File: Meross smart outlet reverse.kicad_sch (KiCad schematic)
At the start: 0 parts

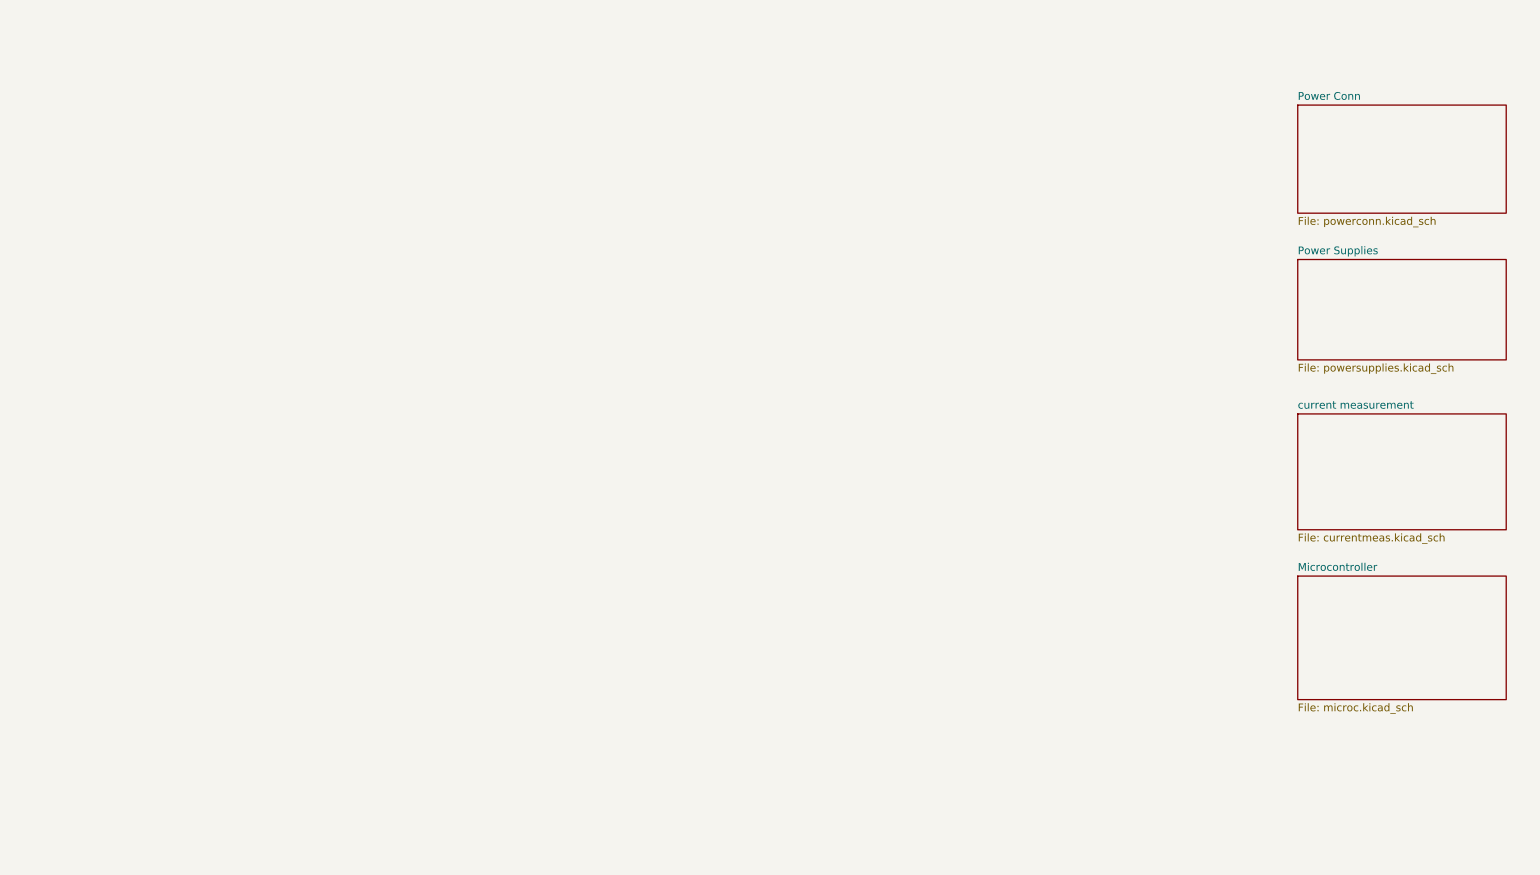
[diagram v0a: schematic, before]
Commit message: Making board layout match better. Added new footprints and symbols.
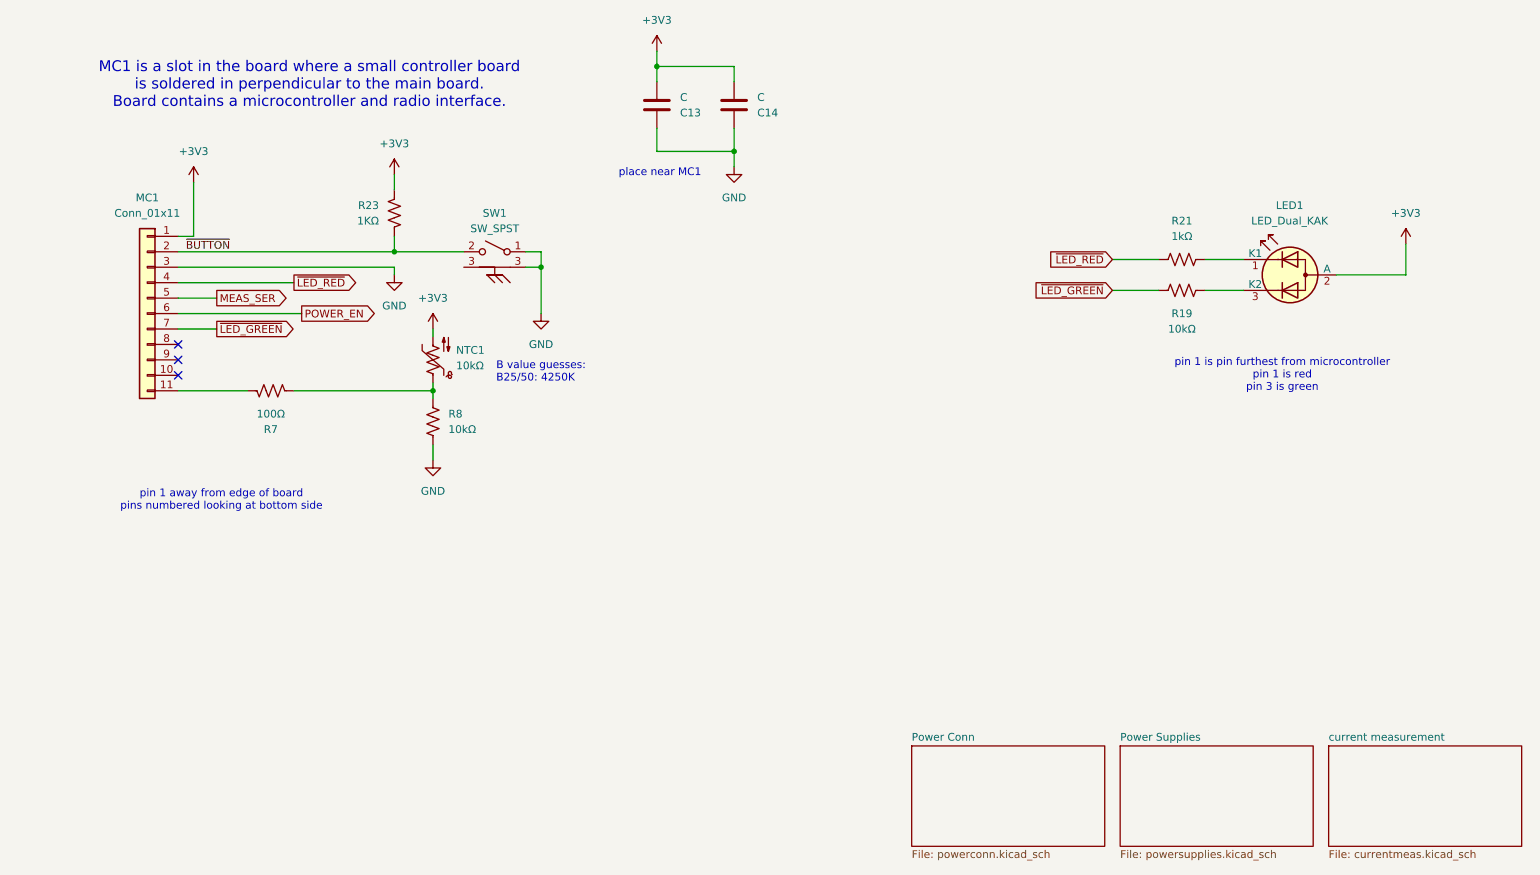
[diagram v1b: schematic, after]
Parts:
- added C13, C14: C, Capacitor_SMD:C_0402_1005Metric, symbol Device:C
- added LED1: LED_Dual_KAK, LED_THT:LED_D3.0mm-3, symbol Device:LED_Dual_KAK
- added MC1: Conn_01x11, HF relays:BoardToBoardInterface_11xP1.00mm, symbol Connector_Generic:Conn_01x11
- added NTC1: 10kΩ, Resistor_SMD:R_0402_1005Metric, symbol Device:Thermistor_NTC_US
- added R19, R8: 10kΩ, Resistor_SMD:R_0402_1005Metric, symbol Device:R_US
- added R21: 1kΩ, Resistor_SMD:R_0402_1005Metric, symbol Device:R_US
- added R23: 1KΩ, Resistor_SMD:R_0402_1005Metric, symbol Device:R_US
- added R7: 100Ω, Resistor_SMD:R_0402_1005Metric, symbol Device:R_US
- added SW1: SW_SPST, HF relays:SW_SPST_Omron_B3F-315x_Angled, symbol merossspecific:SW_SPST_Frame
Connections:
- new net: NTC1.1, R7.2, R8.2
- new net: LED1.1 (K1), R21.2
- new net: LED1.3 (K2), R19.2
- new net: MC1.11 (Pin_11), R7.1
- new net +3V3: C13.2, C14.2, LED1.2 (A), MC1.1 (Pin_1), NTC1.2, R23.1
- new net GND: C13.1, C14.1, MC1.3 (Pin_3), R8.1, SW1.1 (A), SW1.3
- new net MEAS_SER: MC1.5 (Pin_5)
- new net POWER_EN: MC1.6 (Pin_6)
- new net ~{BUTTON}: MC1.2 (Pin_2), R23.2, SW1.2 (B)
- new net ~{LED_GREEN}: MC1.7 (Pin_7), R19.1
- new net ~{LED_RED}: MC1.4 (Pin_4), R21.1
- no-connect marks 0 -> 3
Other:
- removed sheet Microcontroller
- note added: "B value guesses: B25/50: 4250K"
- note added: "MC1 is a slot in the board where a small controller board is soldered in perpendicular to the main board. Board contains a microcontroller and radio interface."
- note added: "pin 1 away from edge of board pins numbered looking at bottom side"
- note added: "pin 1 is pin furthest from microcontroller pin 1 is red pin 3 is green"
- note added: "place near MC1"
- title: (none) -> sensing and controlling interface

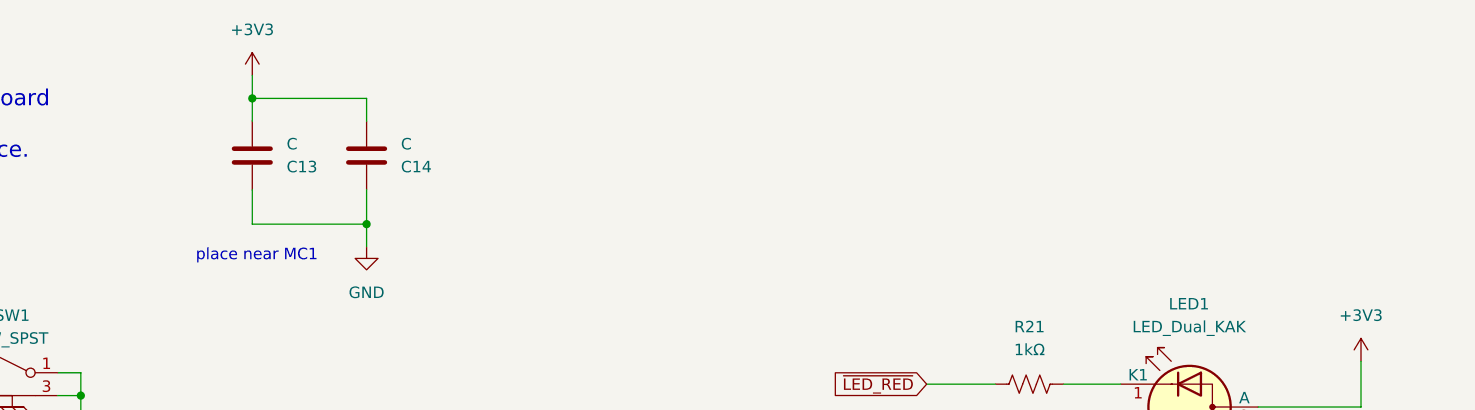
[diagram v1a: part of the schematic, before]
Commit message: All values determined for schematic. From measurements, datasheets, or reading markings.
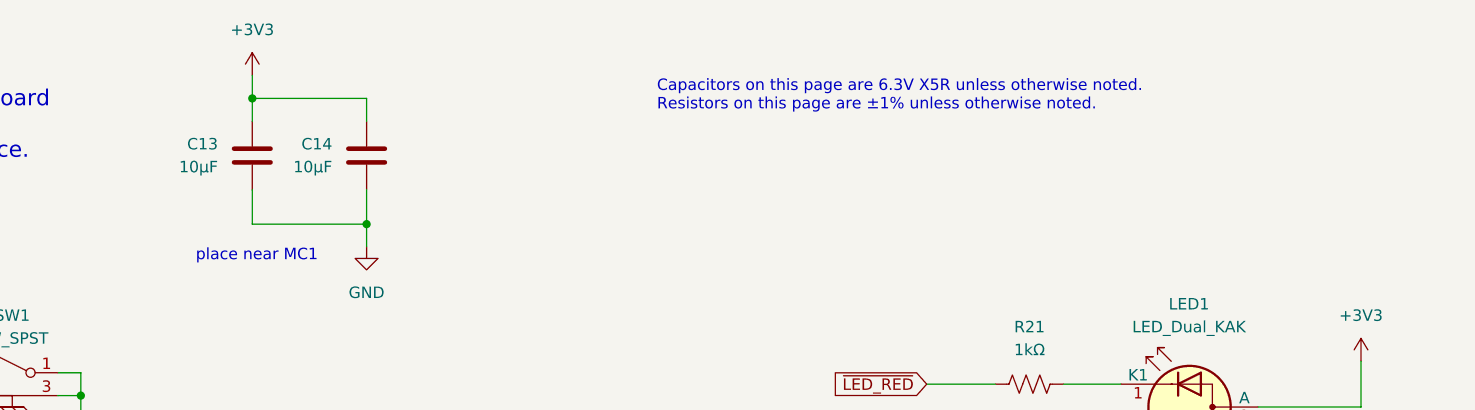
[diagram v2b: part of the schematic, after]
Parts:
- C13, C14: value C -> 10µF
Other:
- note added: "Capacitors on this page are 6.3V X5R unless otherwise noted. Resistors on this page are ±1% unless otherwise noted."
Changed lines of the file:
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@@
+		)
+	)
+	(text "Capacitors on this page are 6.3V X5R unless otherwise noted.\nResistors on this page are ±1% unless otherwise noted."
+		(exclude_from_sim no)
+		(at 161.798 28.956 0)
+		(effects
+			(font
+				(size 1.27 1.27)
+			)
+			(justify left)
 		)
 	)
@@
 		(fields_autoplaced yes)
 		(property "Reference" "C14"
-			(at 133.35 36.8301 0)
-			(effects
-				(font
-					(size 1.27 1.27)
-				)
-				(justify left)
-			)
-		)
-		(property "Value" "C"
-			(at 133.35 34.2901 0)
-			(effects
-				(font
-					(size 1.27 1.27)
-				)
-				(justify left)
+			(at 125.73 34.2899 0)
+			(effects
+				(font
+					(size 1.27 1.27)
+				)
+				(justify right)
+			)
+		)
+		(property "Value" "10µF"
+			(at 125.73 36.8299 0)
+			(effects
+				(font
+					(size 1.27 1.27)
+				)
+				(justify right)
 			)
 		)
@@
 		(fields_autoplaced yes)
 		(property "Reference" "C13"
-			(at 120.65 36.8301 0)
-			(effects
-				(font
-					(size 1.27 1.27)
-				)
-				(justify left)
-			)
-		)
-		(property "Value" "C"
-			(at 120.65 34.2901 0)
-			(effects
-				(font
-					(size 1.27 1.27)
-				)
-				(justify left)
-			)
-		)
+			(at 113.03 34.2899 0)
+			(effects
+				(font
+					(size 1.27 1.27)
+				)
+				(justify right)
+			)
+		)
+		(property "Value" "10µF"
+			(at 113.03 36.8299 0)
+			(effects
+				(font
+					(size 1.27 1.27)
+				)
+				(justify right)
+			)
+		)

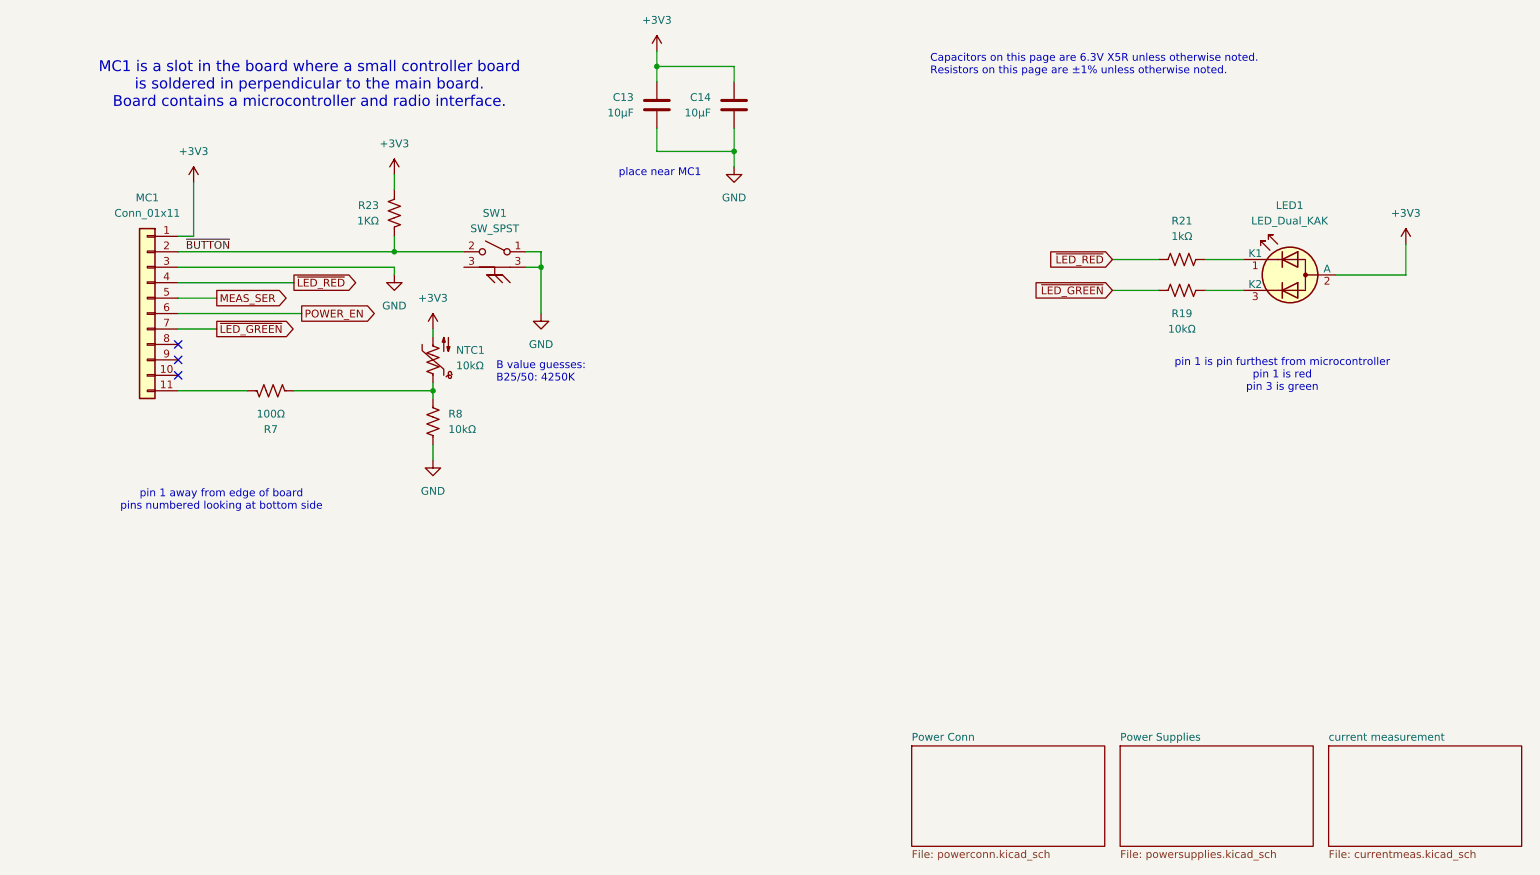
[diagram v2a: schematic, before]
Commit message: Fixed plug and receptacle foots. No components left to fix but L1? And the silk and fab layers. And some kind of labeling of the design.
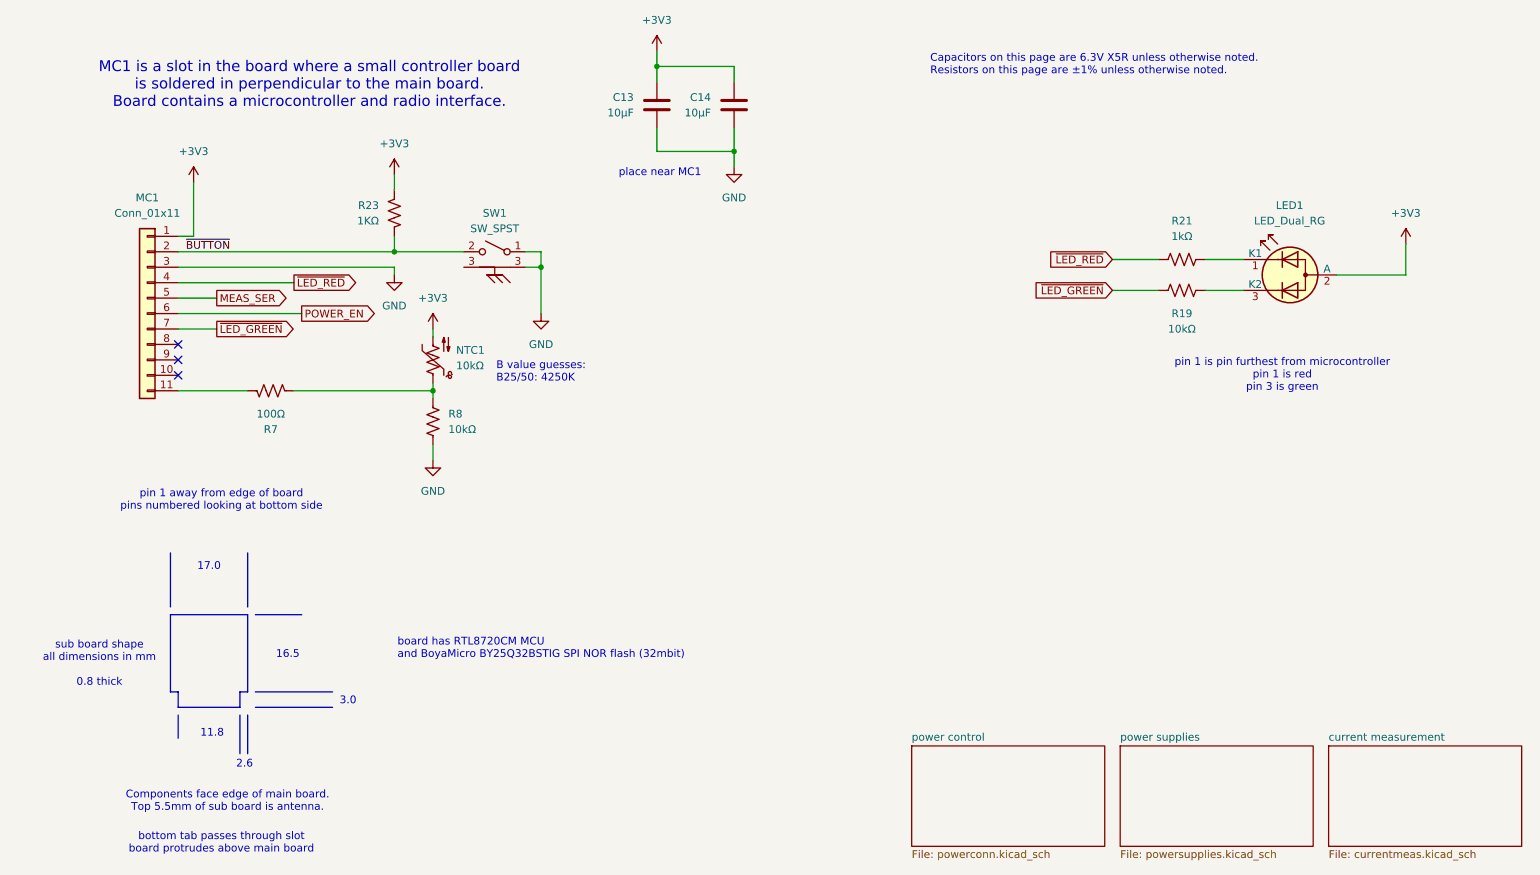
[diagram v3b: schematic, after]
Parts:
- LED1: value LED_Dual_KAK -> LED_Dual_RG; footprint LED_THT:LED_D3.0mm-3 -> HF relays:LED_D3.0mm-3_Horiz
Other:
- sheet Power Conn renamed power control
- sheet Power Supplies renamed power supplies
- note added: "11.8"
- note added: "16.5"
- note added: "17.0"
- note added: "2.6"
- note added: "3.0"
- note added: "Components face edge of main board. Top 5.5mm of sub board is antenna."
- note added: "board has RTL8720CM MCU and BoyaMicro BY25Q32BSTIG SPI NOR flash (32mbit)"
- note added: "bottom tab passes through slot board protrudes above main board"
- note added: "sub board shape all dimensions in mm 0.8 thick"
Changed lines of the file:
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@@
 		(date "2025-07-25")
+	)
+	(text "2.6"
+		(exclude_from_sim no)
+		(at 49.022 144.018 0)
+		(effects
+			(font
+				(size 1.27 1.27)
+			)
+		)
+	)
+	(text "bottom tab passes through slot\nboard protrudes above main board"
+		(exclude_from_sim no)
+		(at 45.212 156.972 0)
+		(effects
+			(font
+				(size 1.27 1.27)
+			)
+		)
+	)
+	(text "11.8"
+		(exclude_from_sim no)
+		(at 43.688 138.938 0)
+		(effects
+			(font
+				(size 1.27 1.27)
+			)
+		)
+	)
+	(text "3.0"
+		(exclude_from_sim no)
+		(at 66.04 133.604 0)
+		(effects
+			(font
+				(size 1.27 1.27)
+			)
+		)
+	)
+	(text "16.5"
+		(exclude_from_sim no)
+		(at 56.134 125.984 0)
+		(effects
+			(font
+				(size 1.27 1.27)
+			)
+		)
 	)
 	(text "place near MC1"
@@
 		)
 	)
+	(text "sub board shape\nall dimensions in mm\n\n0.8 thick"
+		(exclude_from_sim no)
+		(at 25.146 127.508 0)
+		(effects
+			(font
+				(size 1.27 1.27)
+			)
+		)
+	)
 	(text "pin 1 away from edge of board\npins numbered looking at bottom side"
 		(exclude_from_sim no)
@@
 		)
 	)
+	(text "17.0"
+		(exclude_from_sim no)
+		(at 43.18 111.506 0)
+		(effects
+			(font
+				(size 1.27 1.27)
+			)
+		)
+	)
 	(text "pin 1 is pin furthest from microcontroller\npin 1 is red\npin 3 is green\n"
 		(exclude_from_sim no)
@@
 		)
 	)
+	(text "board has RTL8720CM MCU\nand BoyaMicro BY25Q32BSTIG SPI NOR flash (32mbit)"
+		(exclude_from_sim no)
+		(at 74.168 124.968 0)
+		(effects
+			(font
+				(size 1.27 1.27)
+			)
+			(justify left)
+		)
+	)
 	(text "Capacitors on this page are 6.3V X5R unless otherwise noted.\nResistors on this page are ±1% unless otherwise noted."
 		(exclude_from_sim no)
@@
 		)
 	)
+	(text "Components face edge of main board.\nTop 5.5mm of sub board is antenna."
+		(exclude_from_sim no)
+		(at 46.228 150.114 0)
+		(effects
+			(font
+				(size 1.27 1.27)
+			)
+		)
+	)
 	(junction
 		(at 97.79 62.23)
@@
 		)
 	)
+	(polyline
+		(pts
+			(xy 48.26 132.08) (xy 49.53 132.08)
+		)
+		(stroke
+			(width 0)
+			(type default)
+		)
+	)
+	(polyline
+		(pts
+			(xy 36.83 119.38) (xy 36.83 132.08)
+		)
+		(stroke
+			(width 0)
+			(type default)
+		)
+	)
 	(wire
 		(pts
@@
 		)
 	)
+	(polyline
+		(pts
+			(xy 48.26 134.62) (xy 48.26 132.08)
+		)
+		(stroke
+			(width 0)
+			(type default)
+		)
+	)
+	(polyline
+		(pts
+			(xy 50.8 132.08) (xy 63.5 132.08)
+		)
+		(stroke
+			(width 0)
+			(type default)
+		)
+	)
+	(polyline
+		(pts
+			(xy 49.53 135.89) (xy 49.53 142.24)
+		)
+		(stroke
+			(width 0)
+			(type default)
+		)
+	)
+	(polyline
+		(pts
+			(xy 36.83 119.38) (xy 49.53 119.38)
+		)
+		(stroke
+			(width 0)
+			(type default)
+		)
+	)
 	(wire
 		(pts
@@
 		)
 	)
+	(polyline
+		(pts
+			(xy 48.26 135.89) (xy 48.26 142.24)
+		)
+		(stroke
+			(width 0)
+			(type default)
+		)
+	)
 	(wire
 		(pts
@@
 		)
 	)
+	(polyline
+		(pts
+			(xy 38.1 135.89) (xy 38.1 139.7)
+		)
+		(stroke
+			(width 0)
+			(type default)
+		)
+	)
 	(wire
 		(pts
@@
 		)
 	)
+	(polyline
+		(pts
+			(xy 49.53 109.22) (xy 49.53 118.11)
+		)
+		(stroke
+			(width 0)
+			(type default)
+		)
+	)
+	(polyline
+		(pts
+			(xy 50.8 119.38) (xy 58.42 119.38)
+		)
+		(stroke
+			(width 0)
+			(type default)
+		)
+	)
 	(wire
 		(pts
@@
 		)
 	)
+	(polyline
+		(pts
+			(xy 50.8 134.62) (xy 63.5 134.62)
+		)
+		(stroke
+			(width 0)
+			(type default)
+		)
+	)
 	(wire
 		(pts
@@
 		)
 	)
+	(polyline
+		(pts
+			(xy 36.83 132.08) (xy 38.1 132.08)
+		)
+		(stroke
+			(width 0)
+			(type default)
+		)
+	)
 	(wire
 		(pts
@@
 		)
 	)
+	(polyline
+		(pts
+			(xy 49.53 132.08) (xy 49.53 119.38)
+		)
+		(stroke
+			(width 0)
+			(type default)
+		)
+	)
 	(wire
 		(pts
@@
 		)
 	)
+	(polyline
+		(pts
+			(xy 38.1 132.08) (xy 38.1 134.62)
+		)
+		(stroke
+			(width 0)
+			(type default)
+		)
+	)
 	(wire
 		(pts
@@
 		)
 	)
+	(polyline
+		(pts
+			(xy 36.83 109.22) (xy 36.83 118.11)
+		)
+		(stroke
+			(width 0)
+			(type default)
+		)
+	)
 	(wire
 		(pts
 			(xy 38.1 59.69) (xy 73.66 59.69)
+		)
+		(stroke
+			(width 0)
+			(type default)
+		)
+	)
+	(polyline
+		(pts
+			(xy 38.1 134.62) (xy 48.26 134.62)
 		)
 		(stroke
@@
 			)
 		)
-		(property "Value" "LED_Dual_KAK"
+		(property "Value" "LED_Dual_RG"
 			(at 220.9165 54.61 0)
 			(effects
@@
 			)
 		)
-		(property "Footprint" "LED_THT:LED_D3.0mm-3"
+		(property "Footprint" "HF relays:LED_D3.0mm-3_Horiz"
 			(at 219.71 63.5 0)
 			(effects
@@
 			(color 0 0 0 0.0000)
 		)
-		(property "Sheetname" "Power Conn"
+		(property "Sheetname" "power control"
 			(at 158.75 140.2584 0)
 			(effects
@@
 			(color 0 0 0 0.0000)
 		)
-		(property "Sheetname" "Power Supplies"
+		(property "Sheetname" "power supplies"
 			(at 193.04 140.2584 0)
 			(effects
